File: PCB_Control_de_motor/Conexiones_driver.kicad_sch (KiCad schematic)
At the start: 8 parts, among them IC1 DRV8871DDAR

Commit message: Esquemático listo
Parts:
- renumbered C7 to C10, IC1 to IC2, R13 to R12, R14 to R13, R12 to R14
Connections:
- net VM renamed +12V
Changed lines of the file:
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@@
 	(wire
 		(pts
-			(xy 190.5 64.77) (xy 177.8 64.77)
+			(xy 177.8 64.77) (xy 196.85 64.77)
 		)
 		(stroke
@@
 		(pts
 			(xy 123.19 57.15) (xy 127 57.15)
+		)
+		(stroke
+			(width 0)
+			(type default)
+		)
+	)
+	(wire
+		(pts
+			(xy 196.85 64.77) (xy 196.85 63.5)
 		)
 		(stroke
@@
 		)
 	)
-	(hierarchical_label "VM"
-		(shape input)
-		(at 190.5 64.77 0)
-		(effects
-			(font
-				(size 1.27 1.27)
-			)
-			(justify left)
+	(symbol
+		(lib_id "power:+12V")
+		(at 196.85 63.5 0)
+		(unit 1)
+		(exclude_from_sim no)
+		(in_bom yes)
+		(on_board yes)
+		(dnp no)
+		(fields_autoplaced yes)
+		(property "Reference" "#PWR030"
+			(at 196.85 67.31 0)
+			(effects
+				(font
+					(size 1.27 1.27)
+				)
+				(hide yes)
+			)
+		)
+		(property "Value" "+12V"
+			(at 196.85 58.42 0)
+			(effects
+				(font
+					(size 1.27 1.27)
+				)
+			)
+		)
+		(property "Footprint" ""
+			(at 196.85 63.5 0)
+			(effects
+				(font
+					(size 1.27 1.27)
+				)
+				(hide yes)
+			)
+		)
+		(property "Datasheet" ""
+			(at 196.85 63.5 0)
+			(effects
+				(font
+					(size 1.27 1.27)
+				)
+				(hide yes)
+			)
+		)
+		(property "Description" "Power symbol creates a global label with name \"+12V\""
+			(at 196.85 63.5 0)
+			(effects
+				(font
+					(size 1.27 1.27)
+				)
+				(hide yes)
+			)
+		)
+		(pin "1"
+		)
+		(instances
+			(project ""
+				(path "/8d17a2c0-3da6-4d80-8f2f-d7746ccde60e/a462d8b2-121e-4e22-a61f-10de19663ecd"
+					(reference "#PWR030")
+					(unit 1)
+				)
+			)
 		)
 	)
@@
 		(dnp no)
 		(fields_autoplaced yes)
-		(property "Reference" "IC1"
+		(property "Reference" "IC2"
 			(at 142.24 49.53 0)
 			(effects
@@
 			(project ""
 				(path "/8d17a2c0-3da6-4d80-8f2f-d7746ccde60e/a462d8b2-121e-4e22-a61f-10de19663ecd"
-					(reference "IC1")
+					(reference "IC2")
 					(unit 1)
 				)
@@
 		(dnp no)
 		(fields_autoplaced yes)
-		(property "Reference" "#PWR025"
+		(property "Reference" "#PWR026"
 			(at 123.19 85.09 0)
 			(effects
@@
 			(project "PCB_Control_de_motor"
 				(path "/8d17a2c0-3da6-4d80-8f2f-d7746ccde60e/a462d8b2-121e-4e22-a61f-10de19663ecd"
-					(reference "#PWR025")
+					(reference "#PWR026")
 					(unit 1)
 				)
@@
 		(dnp no)
 		(fields_autoplaced yes)
-		(property "Reference" "R14"
+		(property "Reference" "R13"
 			(at 113.03 72.3899 0)
 			(effects
@@
 			(project "PCB_Control_de_motor"
 				(path "/8d17a2c0-3da6-4d80-8f2f-d7746ccde60e/a462d8b2-121e-4e22-a61f-10de19663ecd"
-					(reference "R14")
+					(reference "R13")
 					(unit 1)
 				)
@@
 		(dnp no)
 		(fields_autoplaced yes)
-		(property "Reference" "#PWR026"
+		(property "Reference" "#PWR029"
 			(at 171.45 30.48 0)
 			(effects
@@
 			(project ""
 				(path "/8d17a2c0-3da6-4d80-8f2f-d7746ccde60e/a462d8b2-121e-4e22-a61f-10de19663ecd"
-					(reference "#PWR026")
+					(reference "#PWR029")
 					(unit 1)
 				)
@@
 		(dnp no)
 		(fields_autoplaced yes)
-		(property "Reference" "C7"
+		(property "Reference" "C10"
 			(at 190.5 45.7199 0)
 			(effects
@@
 			(project ""
 				(path "/8d17a2c0-3da6-4d80-8f2f-d7746ccde60e/a462d8b2-121e-4e22-a61f-10de19663ecd"
-					(reference "C7")
+					(reference "C10")
 					(unit 1)
 				)
@@
 		(dnp no)
 		(fields_autoplaced yes)
-		(property "Reference" "#PWR023"
+		(property "Reference" "#PWR024"
 			(at 104.14 86.36 0)
 			(effects
@@
 			(project ""
 				(path "/8d17a2c0-3da6-4d80-8f2f-d7746ccde60e/a462d8b2-121e-4e22-a61f-10de19663ecd"
-					(reference "#PWR023")
+					(reference "#PWR024")
 					(unit 1)
 				)
@@
 		(dnp no)
 		(fields_autoplaced yes)
-		(property "Reference" "R12"
+		(property "Reference" "R14"
 			(at 125.73 72.3899 0)
 			(effects
@@
 			(project ""
 				(path "/8d17a2c0-3da6-4d80-8f2f-d7746ccde60e/a462d8b2-121e-4e22-a61f-10de19663ecd"
-					(reference "R12")
+					(reference "R14")
 					(unit 1)
 				)
@@
 		(dnp no)
 		(fields_autoplaced yes)
-		(property "Reference" "#PWR07"
+		(property "Reference" "#PWR028"
 			(at 170.18 91.44 0)
 			(effects
@@
 			(project ""
 				(path "/8d17a2c0-3da6-4d80-8f2f-d7746ccde60e/a462d8b2-121e-4e22-a61f-10de19663ecd"
-					(reference "#PWR07")
+					(reference "#PWR028")
 					(unit 1)
 				)
@@
 		(dnp no)
 		(fields_autoplaced yes)
-		(property "Reference" "R13"
+		(property "Reference" "R12"
 			(at 100.33 72.3899 0)
 			(effects
@@
 			(project ""
 				(path "/8d17a2c0-3da6-4d80-8f2f-d7746ccde60e/a462d8b2-121e-4e22-a61f-10de19663ecd"
-					(reference "R13")
+					(reference "R12")
 					(unit 1)
 				)
@@
 		(dnp no)
 		(fields_autoplaced yes)
-		(property "Reference" "#PWR024"
+		(property "Reference" "#PWR025"
 			(at 123.19 48.26 0)
 			(effects
@@
 			(project "PCB_Control_de_motor"
 				(path "/8d17a2c0-3da6-4d80-8f2f-d7746ccde60e/a462d8b2-121e-4e22-a61f-10de19663ecd"
-					(reference "#PWR024")
+					(reference "#PWR025")
 					(unit 1)
 				)

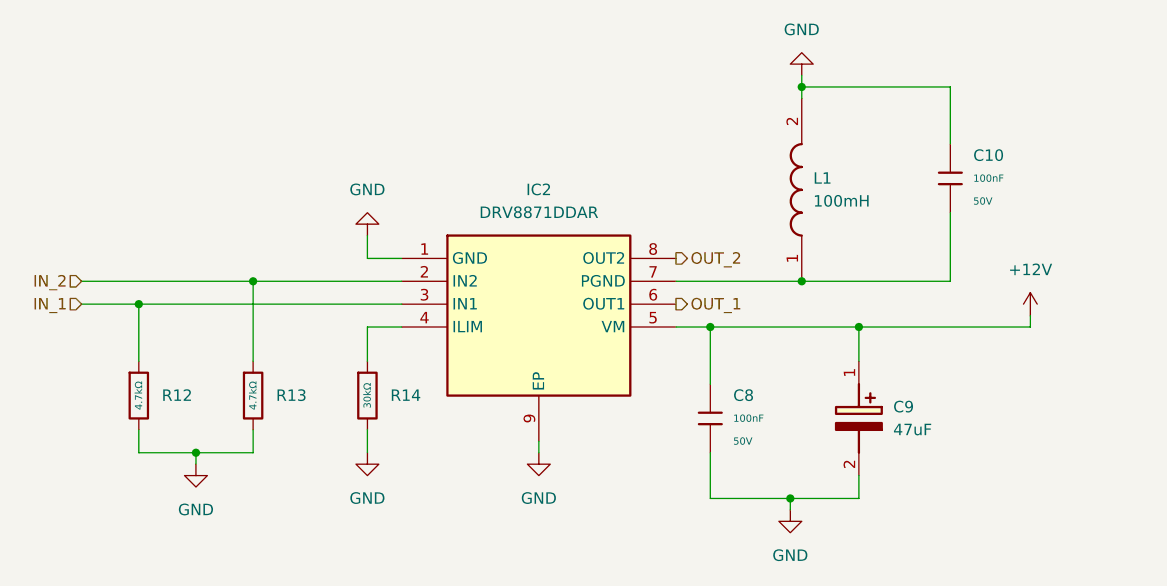
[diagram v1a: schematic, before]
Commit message: Corrección 3 del esquemático
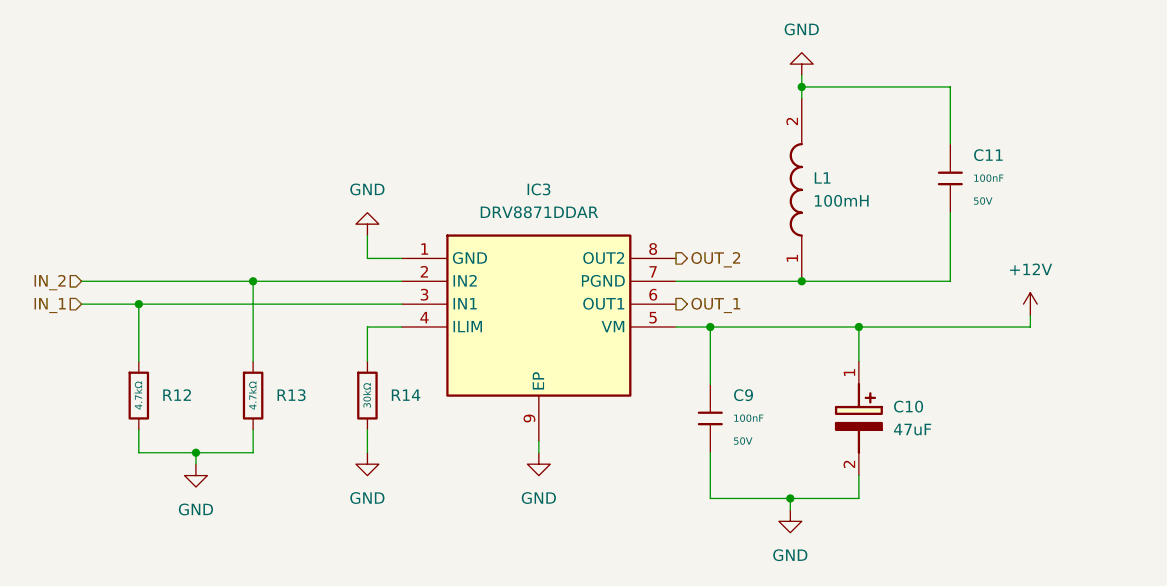
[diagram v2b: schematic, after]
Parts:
- renumbered C9 to C10, C10 to C11, C8 to C9, IC2 to IC3
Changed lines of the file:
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@@
 		(dnp no)
 		(fields_autoplaced yes)
-		(property "Reference" "C8"
+		(property "Reference" "C9"
 			(at 163.83 72.3899 0)
 			(effects
@@
 			(project "PCB_Control_de_motor"
 				(path "/8d17a2c0-3da6-4d80-8f2f-d7746ccde60e/a462d8b2-121e-4e22-a61f-10de19663ecd"
-					(reference "C8")
+					(reference "C9")
 					(unit 1)
 				)
@@
 		(dnp no)
 		(fields_autoplaced yes)
-		(property "Reference" "IC2"
+		(property "Reference" "IC3"
 			(at 142.24 49.53 0)
 			(effects
@@
 			(project ""
 				(path "/8d17a2c0-3da6-4d80-8f2f-d7746ccde60e/a462d8b2-121e-4e22-a61f-10de19663ecd"
-					(reference "IC2")
+					(reference "IC3")
 					(unit 1)
 				)
@@
 		(dnp no)
 		(fields_autoplaced yes)
-		(property "Reference" "C9"
+		(property "Reference" "C10"
 			(at 181.61 73.6599 90)
 			(effects
@@
 			(project ""
 				(path "/8d17a2c0-3da6-4d80-8f2f-d7746ccde60e/a462d8b2-121e-4e22-a61f-10de19663ecd"
-					(reference "C9")
+					(reference "C10")
 					(unit 1)
 				)
@@
 		(dnp no)
 		(fields_autoplaced yes)
-		(property "Reference" "C10"
+		(property "Reference" "C11"
 			(at 190.5 45.7199 0)
 			(effects
@@
 			(project ""
 				(path "/8d17a2c0-3da6-4d80-8f2f-d7746ccde60e/a462d8b2-121e-4e22-a61f-10de19663ecd"
-					(reference "C10")
+					(reference "C11")
 					(unit 1)
 				)

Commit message: PCB casi terminado
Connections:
- net GND: no longer C10.2 (-)
- net at C11.2, IC3.7 (PGND), L1.1: now also C10.2 (-)
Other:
- moved on the sheet: C10, C9

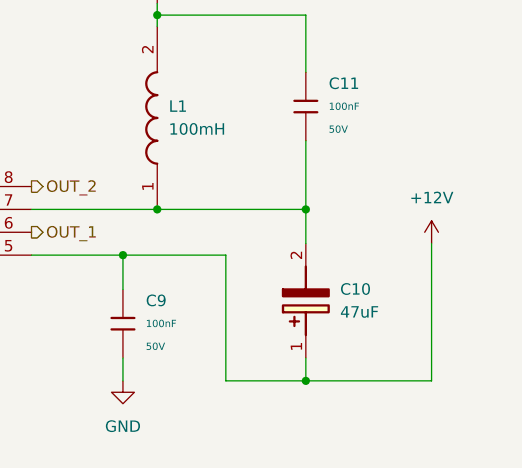
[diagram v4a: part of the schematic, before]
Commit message: Cambio del capacitor y rediseño de las pistas del driver con sus componentes
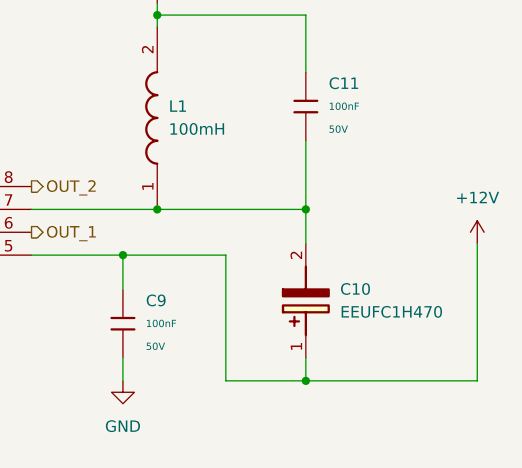
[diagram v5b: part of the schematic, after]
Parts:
- removed C10: 47uF, SamacSys_Parts:CAPAE660X820N, symbol SamacSys_Parts:RVT1H470M0607
- added C10: EEUFC1H470, SamacSys_Parts:CAPPRD250W55D630H1220, symbol SamacSys_Parts:EEUFC1H470
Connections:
- net +12V: now also C10.1 (+)
- net at C11.2, IC3.7 (PGND), L1.1: now also C10.2 (-)
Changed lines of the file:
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@@
 	(wire
 		(pts
-			(xy 201.93 78.74) (xy 201.93 63.5)
+			(xy 207.01 78.74) (xy 207.01 63.5)
 		)
 		(stroke
@@
 	(wire
 		(pts
-			(xy 187.96 78.74) (xy 201.93 78.74)
+			(xy 187.96 78.74) (xy 207.01 78.74)
 		)
 		(stroke
@@
 	(symbol
 		(lib_id "power:+12V")
-		(at 201.93 63.5 0)
+		(at 207.01 63.5 0)
 		(unit 1)
 		(exclude_from_sim no)
@@
 		(fields_autoplaced yes)
 		(property "Reference" "#PWR035"
-			(at 201.93 67.31 0)
+			(at 207.01 67.31 0)
 			(effects
 				(font
@@
 		)
 		(property "Value" "+12V"
-			(at 201.93 58.42 0)
+			(at 207.01 58.42 0)
 			(effects
 				(font
@@
 		)
 		(property "Footprint" ""
-			(at 201.93 63.5 0)
+			(at 207.01 63.5 0)
 			(effects
 				(font
@@
 		)
 		(property "Datasheet" ""
-			(at 201.93 63.5 0)
+			(at 207.01 63.5 0)
 			(effects
 				(font
@@
 		)
 		(property "Description" "Power symbol creates a global label with name \"+12V\""
-			(at 201.93 63.5 0)
+			(at 207.01 63.5 0)
 			(effects
 				(font
@@
 	)
 	(symbol
-		(lib_id "SamacSys_Parts:RVT1H470M0607")
+		(lib_id "SamacSys_Parts:EEUFC1H470")
 		(at 187.96 76.2 90)
 		(unit 1)
@@
 			)
 		)
-		(property "Value" "47uF"
+		(property "Value" "EEUFC1H470"
 			(at 191.77 71.1199 90)
 			(effects
@@
 			)
 		)
-		(property "Footprint" "SamacSys_Parts:CAPAE660X820N"
+		(property "Footprint" "SamacSys_Parts:CAPPRD250W55D630H1220"
 			(at 284.15 67.31 0)
 			(effects
@@
 			)
 		)
-		(property "Datasheet" ""
+		(property "Datasheet" "http://industrial.panasonic.com/cdbs/www-data/pdf/RDF0000/ABA0000C1209.pdf"
 			(at 384.15 67.31 0)
 			(effects
@@
 			)
 		)
-		(property "Description" "Aluminum Electrolytic Capacitors - SMD 47uF +/-20% 50V SMD,6.3x7.7mm RoHS"
+		(property "Description" "Aluminium Electrolytic Capacitor, Radial Lead, AEC-Q200, 105?C 50v,47uf"
 			(at 187.96 76.2 0)
 			(effects
@@
 			)
 		)
-		(property "Height" "8.2"
+		(property "Height" "12.2"
 			(at 584.15 67.31 0)
 			(effects
@@
 			)
 		)
-		(property "Manufacturer_Name" "ROQANG"
+		(property "Manufacturer_Name" "Panasonic"
 			(at 684.15 67.31 0)
 			(effects
@@
 			)
 		)
-		(property "Manufacturer_Part_Number" "RVT1H470M0607"
+		(property "Manufacturer_Part_Number" "EEUFC1H470"
 			(at 784.15 67.31 0)
 			(effects
